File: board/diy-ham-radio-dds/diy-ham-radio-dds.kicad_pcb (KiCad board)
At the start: 2 copper layers, 150 x 50 mm, 63 parts, among them J1 ICSP, J2 I2C, J3 VCC, J4 NPN OUT, J5 , J6 UART_PROG, Q1 S0805, Q2 S0805, Q3 S0805, Q4 S0805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

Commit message: Changed NPN out channels in schematics
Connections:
- U4 pad 15: Q1_NPN -> Q6_NPN
- U4 pad 2: Q3_NPN -> Q1_NPN
- U4 pad 3: Q4_NPN -> Q3_NPN
- U4 pad 5: Q6_NPN -> Q4_NPN
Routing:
- net Q1_NPN: track 53.1 -> 57.6 mm, vias 1 -> 2
- net Q6_NPN: track 39.5 -> 42.8 mm
- net Q3_NPN: track 55.4 -> 58.1 mm, vias 1 -> 2
- net Q4_NPN: track 46.5 -> 49.0 mm, vias 1 -> 2
- net (no net): track 0.10 -> 0.00 mm, vias 7 -> 4

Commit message: Finalised board drawing
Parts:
- C1, C10, C11, C13, C5, C6, C9, R11, R12, R13, R18, R19, R2, R20, R3, R6: moved to B.Cu
- J1: footprint Connector_PinHeader_1.00mm:PinHeader_2x03_P1.00mm_Vertical -> Connector_PinHeader_2.54mm:PinHeader_2x03_P2.54mm_Vertical; moved to B.Cu
- J2, J3: footprint Connector_PinHeader_1.00mm:PinHeader_2x04_P1.00mm_Vertical -> Connector_PinHeader_2.54mm:PinHeader_2x04_P2.54mm_Vertical; moved to B.Cu
- J6: footprint Connector_PinHeader_1.27mm:PinHeader_1x06_P1.27mm_Vertical -> Connector_PinHeader_2.54mm:PinHeader_1x06_P2.54mm_Vertical; moved to B.Cu
- RV1: footprint Potentiometer_THT:Potentiometer_Alpha_RD901F-40-00D_Single_Vertical -> Potentiometer_THT:Potentiometer_Bourns_3296W_Vertical; moved to B.Cu
- U3: footprint Package_TO_SOT_THT:TO-220-3_Vertical -> Package_TO_SOT_THT:TO-220-3_Horizontal_TabDown
- moved C10 137.6 mm to (138.6, 114.6), turned to 270 degrees
- moved RV1 107.2 mm to (142.6, 113.8), turned to 180 degrees
- moved R6 98.2 mm to (175.0, 114.5), turned to 270 degrees
- moved C13 77.9 mm to (275.1, 113.0), turned to 90 degrees
- moved R2 66.0 mm to (235.3, 128.6), turned to 270 degrees
- moved C9 65.3 mm to (261.8, 126.6), turned to 270 degrees
- moved C11 63.0 mm to (261.8, 123.5), turned to 90 degrees
- moved J2 60.4 mm to (232.7, 125.5)
- moved C5 59.4 mm to (217.2, 145.9)
- moved C1 58.7 mm to (213.2, 144.8)
- moved C6 57.8 mm to (216.9, 144.0), turned to 180 degrees
- moved R3 54.8 mm to (232.7, 128.6), turned to 270 degrees
- moved R11 53.2 mm to (215.8, 149.0)
- moved U3 49.8 mm to (210.8, 141.9)
- moved R13 49.3 mm to (215.8, 151.5)
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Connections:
- J5 pad 1: POT2_A -> POT2_C
- J5 pad 10: Net-(J5-Pad10) -> GND
- J5 pad 3: POT2_C -> POT2_A
- J5 pad 4: POT1_A -> POT1_C
- J5 pad 6: POT1_C -> POT1_A
- J5 pad 9: Net-(J5-Pad9) -> VIN
- U1 pad 19: POT_1 -> POT_2
- U1 pad 22: POT_2 -> POT_1
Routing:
- net VCC: track 128.6 -> 402.6 mm, vias 0 -> 7
- net PTT: track 0.00 -> 117.8 mm, vias 0 -> 4
- net ALARM: track 0.00 -> 114.9 mm, vias 0 -> 4
- net DISP_D4: track 328.1 -> 214.2 mm
- net RST: track 31.7 -> 117.0 mm
- net POT2_B: track 0.00 -> 66.5 mm
- net POT2_C: track 0.00 -> 65.7 mm
- net POT2_A: track 0.00 -> 64.8 mm
- net POT1_B: track 0.00 -> 40.6 mm, vias 0 -> 1
- net POT1_A: track 0.00 -> 39.0 mm, vias 0 -> 1
- net DISP_EN: track 164.5 -> 202.7 mm, vias 1 -> 3
- net POT1_C: track 0.00 -> 35.9 mm
- net SCL: track 23.3 -> 55.1 mm
- net SDA: track 23.2 -> 50.7 mm
- net POT_1: track 39.0 -> 66.0 mm
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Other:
- outline, holes or cut-outs redrawn

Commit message: DRC-Cleared for JLCPCB Production
Used https://github.com/sethhillbrand/kicad_templates
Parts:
- U3: moved to B.Cu
- moved C5 5.62 mm to (211.6, 145.4)
- moved C6 5.62 mm to (211.3, 143.5)
- moved U3 5.15 mm to (215.9, 141.2), turned to 180 degrees
- moved C1 2.97 mm to (211.6, 147.3)
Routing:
- net VCC: track 402.6 -> 413.5 mm
- net VIN: track 21.3 -> 30.9 mm
- net GND: vias 238 -> 236
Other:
- copper layers 2 -> 4
- net class Default: clearance 0.2 -> 0.127; trace_width 0.25 -> 0.127; via_dia 0.8 -> 0.6; via_drill 0.4 -> 0.3
- rule trace_clearance: 0.2 -> 0.127
- rule trace_min: 0.2 -> 0.127
- rule via_min_size: 0.4 -> 0.6

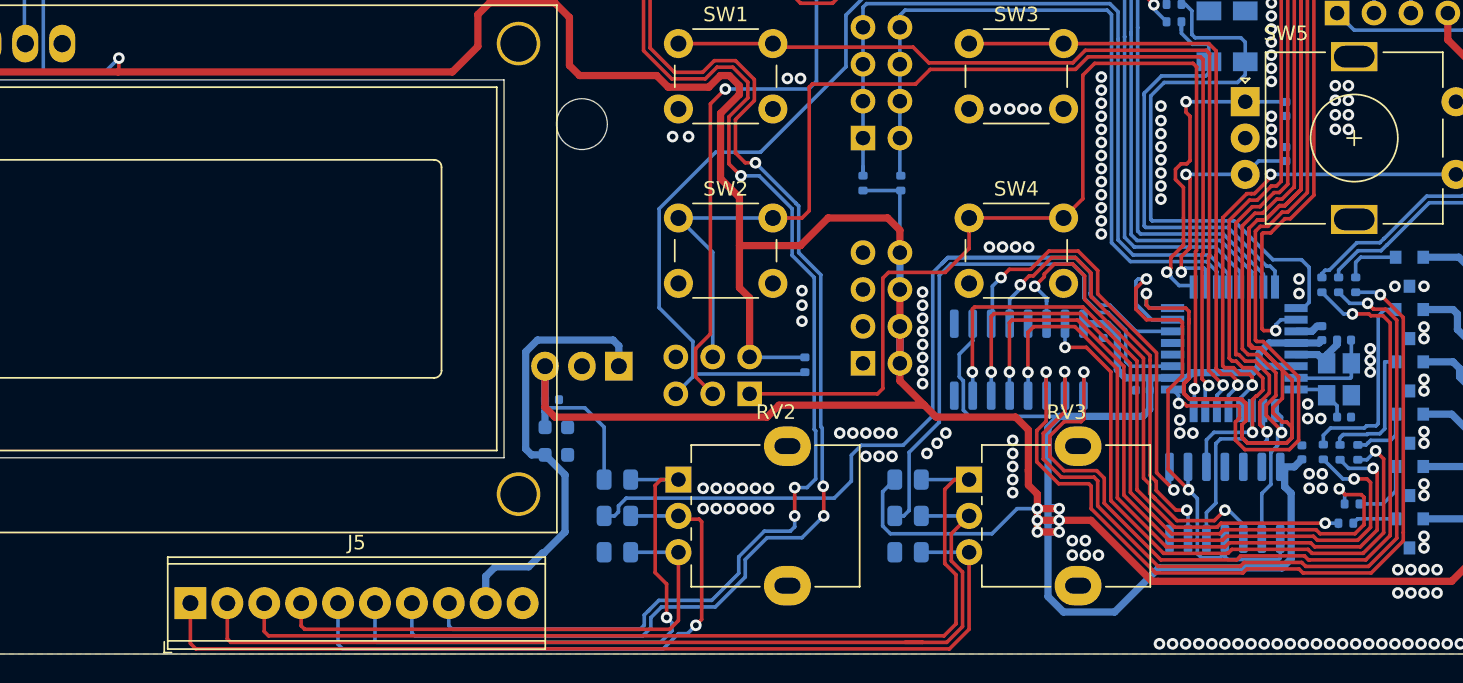
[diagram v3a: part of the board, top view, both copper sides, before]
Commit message: Added more tolerance to LCD cutout
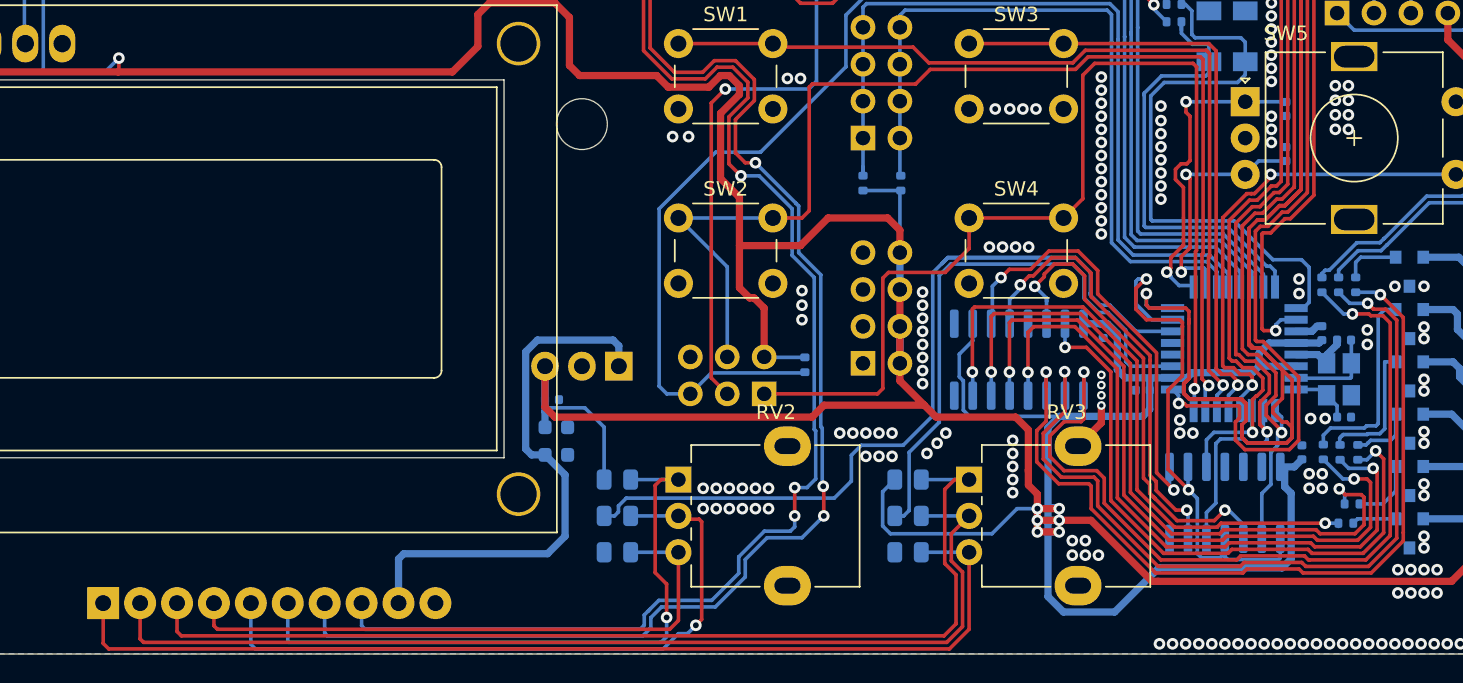
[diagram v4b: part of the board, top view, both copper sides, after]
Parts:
- J5: moved to B.Cu
- moved J5 6.00 mm to (180.4, 157.5)
- moved J1 1.00 mm to (225.9, 143.1)
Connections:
- DS1 pad : (no net) -> GND
- RV2 pad : (no net) -> GND
- RV3 pad : (no net) -> GND
- SW5 pad MP: (no net) -> GND
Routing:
- net VIN: track 30.9 -> 37.8 mm
- net POT2_C: track 65.7 -> 71.7 mm
- net POT1_C: track 35.9 -> 41.9 mm
- net POT1_B: track 40.6 -> 46.6 mm
- net ALARM: track 114.9 -> 120.9 mm
- net PTT: track 117.8 -> 123.8 mm
- net POT2_A: track 64.8 -> 70.8 mm
- net POT1_A: track 39.0 -> 44.7 mm
- net POT2_B: track 66.5 -> 71.3 mm
- net GND: track 6.74 -> 10.2 mm, vias 236 -> 238
- net SW4: track 74.7 -> 73.7 mm
- net RST: track 117.0 -> 117.7 mm
